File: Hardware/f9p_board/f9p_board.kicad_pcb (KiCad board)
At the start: 4 copper layers, 75 x 41 mm, 94 parts, among them J1 USB_B_Mini, J2 USB_B_Mini, J3 BAT_CONN, J4 CAN, J5 USB_A_PWR_OUTPUT, J6 EN_BAT_VIN, J7 SERV_0, J8 SERV_1, P1 SWD, Q1 DMN62D0UW-7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

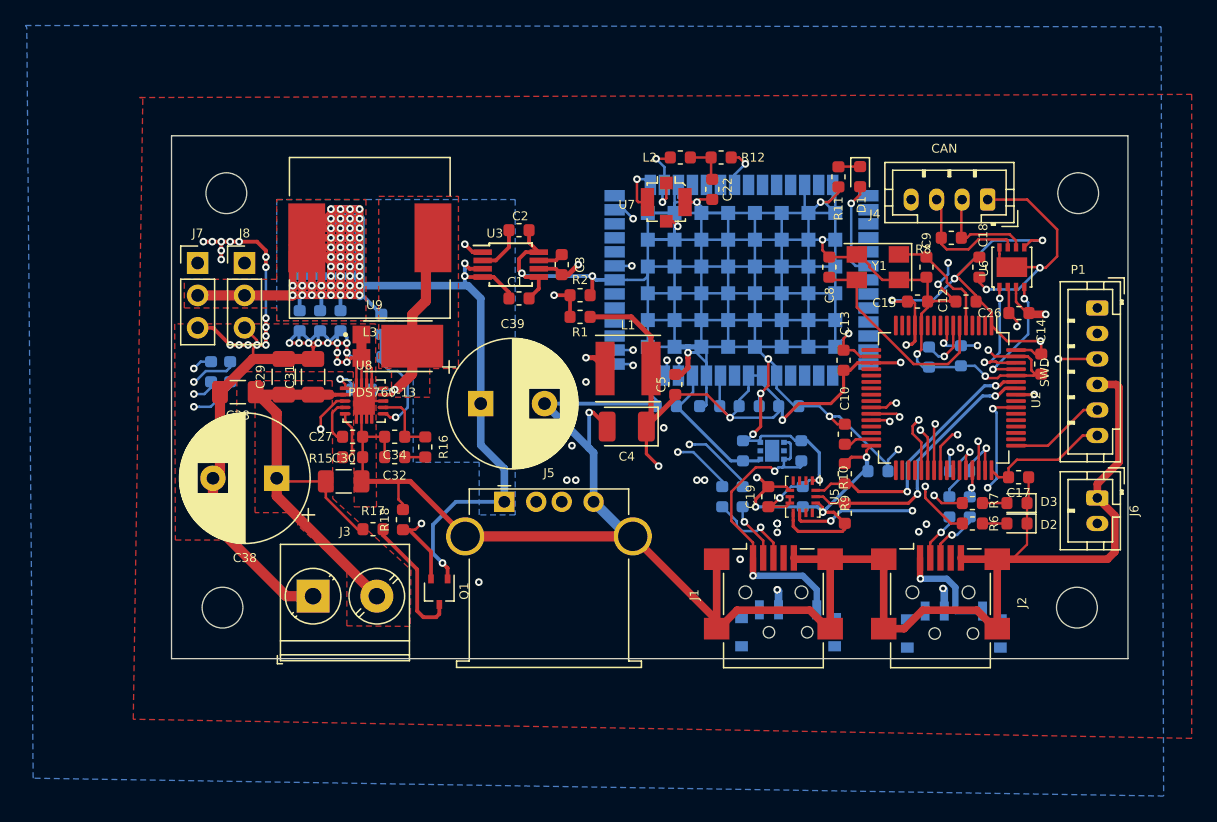
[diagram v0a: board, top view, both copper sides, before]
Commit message: f9p_board: Added switch for boot0 to enable USB flashing. Added another pair of servo connectors
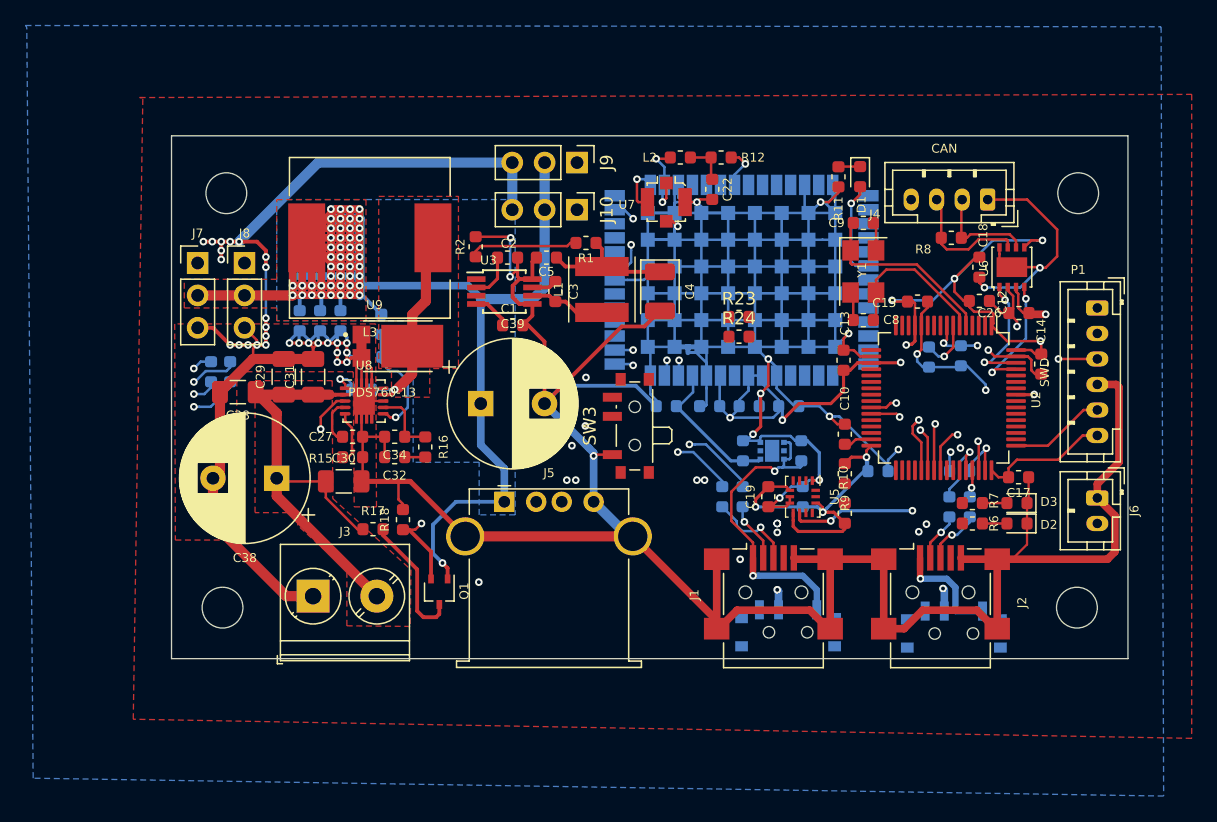
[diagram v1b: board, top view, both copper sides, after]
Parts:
- added J10: SERV_3, Connector_PinHeader_2.54mm:PinHeader_1x03_P2.54mm_Vertical, F.Cu at (76.8, 58.8)
- added J9: SERV_2, Connector_PinHeader_2.54mm:PinHeader_1x03_P2.54mm_Vertical, F.Cu at (76.8, 55.1)
- added R23: 220R, Resistor_SMD:R_0603_1608Metric, F.Cu at (89.5, 67.2)
- added R24: 220R, Resistor_SMD:R_0603_1608Metric, F.Cu at (89.5, 68.8)
- added SW3: BOOT0, Button_Switch_SMD:SW_SPDT_PCM12, F.Cu at (81.0, 75.8)
- moved C5 14.2 mm to (74.4, 62.5), turned to 180 degrees
- moved C4 10.9 mm to (83.3, 65.2), turned to -90 degrees
- moved R2 9.03 mm to (68.8, 61.7), turned to -90 degrees
- moved L1 6.53 mm to (78.8, 65.0), turned to -90 degrees
- moved C9 6.05 mm to (99.2, 59.8), turned to 180 degrees
- moved R1 5.82 mm to (77.5, 61.4)
- moved C8 4.93 mm to (99.2, 67.5), turned to 0 degrees
- moved C2 2.33 mm to (71.3, 62.5)
- moved C3 2.17 mm to (75.1, 65.2)
- moved U3 2.17 mm to (71.1, 65.2)
- moved C1 2.17 mm to (71.8, 67.9)
- moved Y1 1.19 mm to (99.2, 63.6), turned to -90 degrees
- moved C12 1.05 mm to (108.3, 66.0), turned to 0 degrees
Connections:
- U2 pad 16: Net-(U2-Pad16) -> SERV_2
- U2 pad 17: Net-(U2-Pad17) -> SERV_3
- U2 pad 28: LED0 -> GND
- U2 pad 29: Net-(U2-Pad29) -> SCL
- U2 pad 30: Net-(U2-Pad30) -> SDA
- U2 pad 42: Net-(U2-Pad42) -> PWR_5V
- U2 pad 51: Net-(U2-Pad51) -> LED0
- U2 pad 52: Net-(U2-Pad52) -> LED1
- U2 pad 55: LED1 -> Net-(U2-Pad55)
- U2 pad 58: SCL -> Net-(U2-Pad58)
- U2 pad 59: SDA -> Net-(U2-Pad59)
- U2 pad 60: GND -> Net-(SW3-Pad2)
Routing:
- net GND: track 622.0 -> 650.7 mm, vias 54 -> 50
- net VCC: track 151.6 -> 129.1 mm, vias 13 -> 11
- net SCL: track 21.2 -> 0.00 mm, vias 2 -> 0
- net SDA: track 21.1 -> 0.00 mm, vias 2 -> 0
- net LED1: track 15.4 -> 0.00 mm, vias 3 -> 0
- net LED0: track 12.4 -> 0.00 mm, vias 2 -> 0
- net PWR_5V: track 346.0 -> 356.5 mm, vias 63 -> 61
- net Net-(C3-Pad2): track 13.0 -> 5.99 mm, vias 2 -> 0
- net Net-(C9-Pad2): track 9.27 -> 14.9 mm
- net Net-(R1-Pad1): track 13.3 -> 8.57 mm, vias 2 -> 0
- net Net-(C8-Pad2): track 16.8 -> 12.5 mm
- net F9P_RESET_N: track 36.6 -> 38.8 mm
- net CAN_TX: track 9.21 -> 9.76 mm
- net Net-(R22-Pad2): track 63.2 -> 62.6 mm

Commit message: f9p_board: routing
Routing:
- net GND: track 650.7 -> 726.5 mm, vias 50 -> 110
- net Net-(SW3-Pad2): track 0.00 -> 35.8 mm, vias 0 -> 3
- net VCC: track 129.1 -> 160.1 mm, vias 11 -> 13
- net Net-(J9-Pad1): track 0.00 -> 18.7 mm
- net Net-(J10-Pad1): track 0.00 -> 18.0 mm
- net LED0: track 0.00 -> 14.1 mm, vias 0 -> 2
- net SERV_2: track 0.00 -> 12.4 mm
- net SCL: track 0.00 -> 11.4 mm
- net LED1: track 0.00 -> 10.1 mm, vias 0 -> 2
- net SERV_3: track 0.00 -> 10.0 mm
- net SDA: track 0.00 -> 9.46 mm
- net PWR_5V: track 356.5 -> 364.5 mm, vias 61 -> 62
- net Net-(R1-Pad1): track 8.57 -> 10.3 mm
- net MCU_TX_F9P_RX: track 31.7 -> 31.1 mm

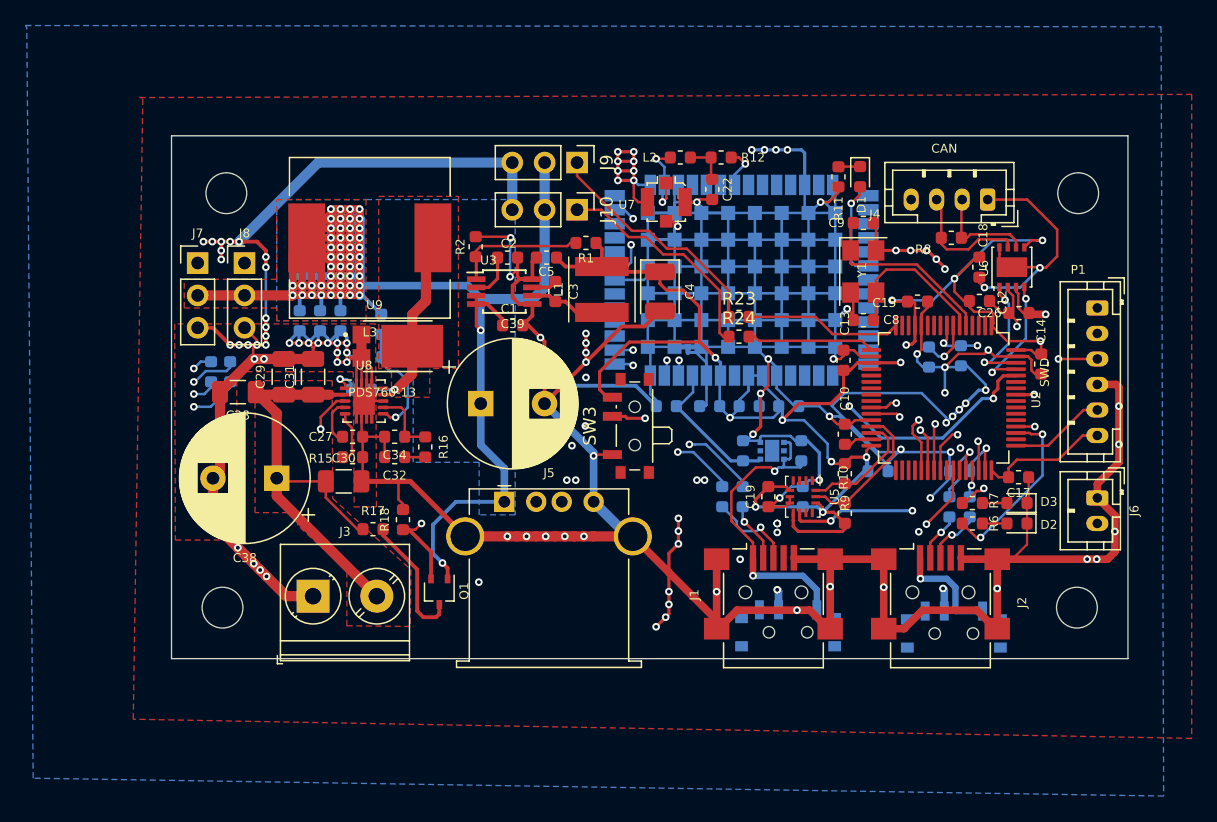
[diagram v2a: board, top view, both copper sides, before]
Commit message: f9p_board:  internal copper layers are GND
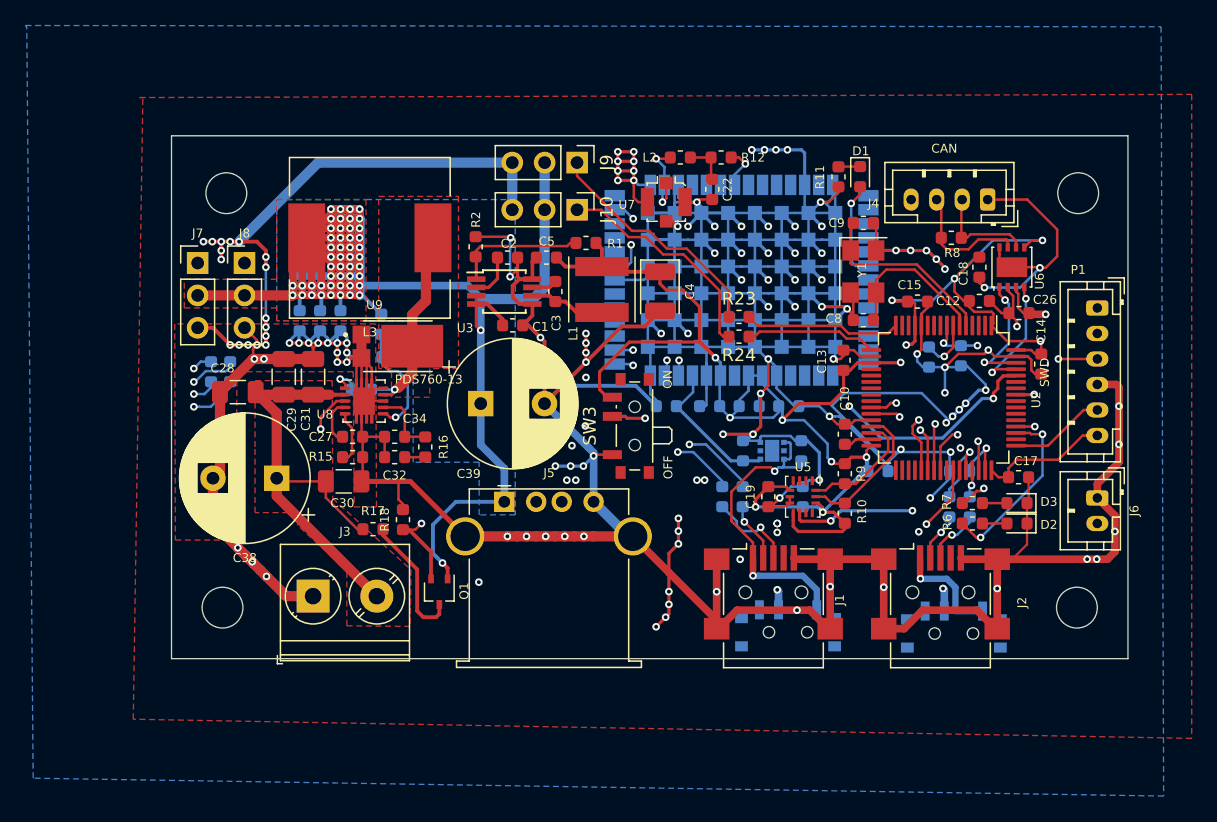
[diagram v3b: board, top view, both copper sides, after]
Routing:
- net GND: track 726.5 -> 759.0 mm, vias 110 -> 133
- added copper zone on F.Cu, net (none)
- removed copper zone on F.Cu, net SW

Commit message: Finished F9P PCB v1.0
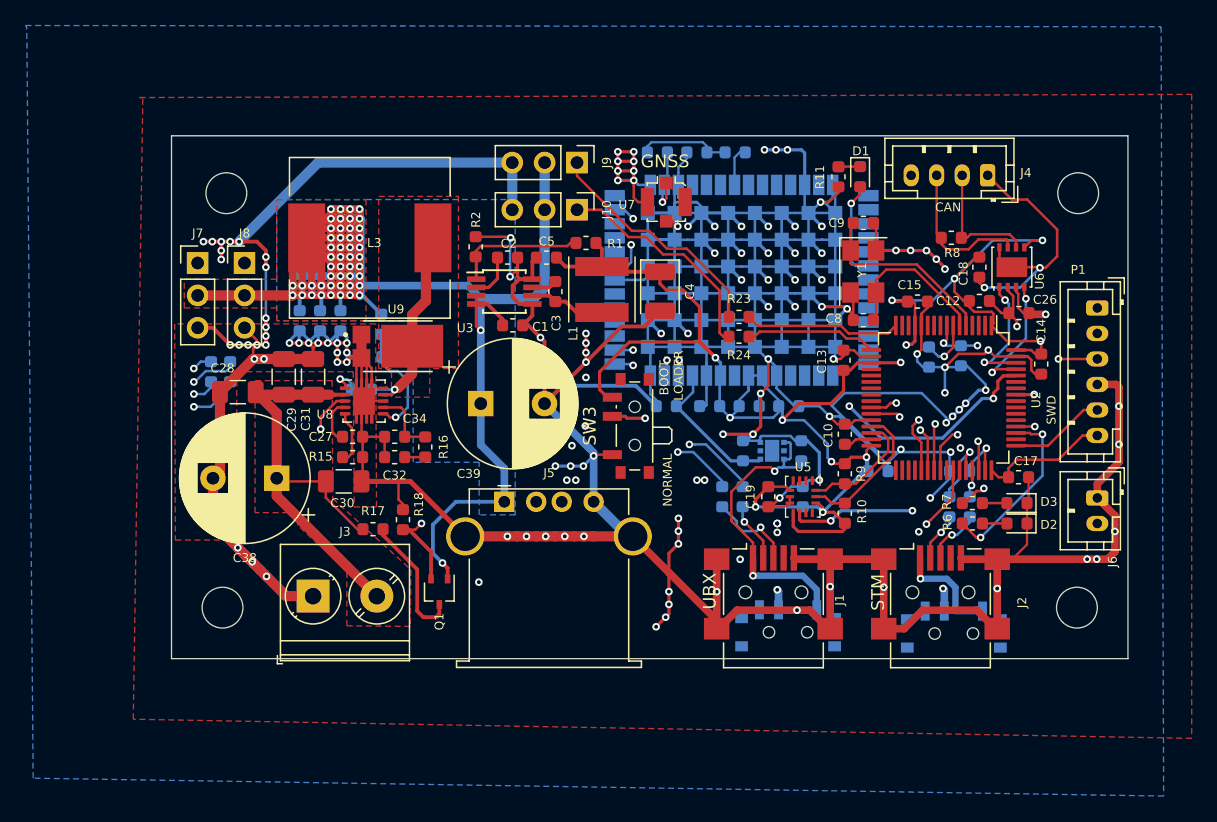
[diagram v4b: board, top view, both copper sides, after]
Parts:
- C22, L2, R12: moved to B.Cu
- moved C22 3.14 mm to (86.2, 54.3), turned to 180 degrees
- moved J4 1.90 mm to (109.0, 56.1)
- moved L2 1.84 mm to (83.1, 54.3), turned to 180 degrees
- moved R12 1.17 mm to (89.2, 54.3)
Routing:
- net Net-(C22-Pad1): track 3.37 -> 7.32 mm
- net PWR_5V: track 364.5 -> 367.5 mm
- net CANL: track 8.16 -> 10.1 mm
- net CANH: track 10.2 -> 12.1 mm
- net Net-(L2-Pad1): track 6.51 -> 5.80 mm, vias 2 -> 1
- net GND: track 759.0 -> 759.4 mm, vias 133 -> 131
- net Net-(R12-Pad1): track 3.32 -> 3.15 mm, vias 1 -> 0
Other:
- board text added: "(RX)"
- board text added: "(TX)"
- board text added: "5V"
- board text added: "7-60V"
- board text added: "BOOT- LOADER"
- board text added: "CANH"
- board text added: "CANL"
- board text added: "CarController v1.0"
- board text added: "GND"
- board text added: "GNSS"
- board text added: "Joel Svensson Benjamin Vedder"
- board text added: "NORMAL"
- board text added: "NRST"
- board text added: "PWR_OFF"
- board text added: "S"
- board text added: "STM"
- board text added: "SWCLK"
- board text added: "SWDIO"
- board text added: "UBX"
- board text added: "VCC"

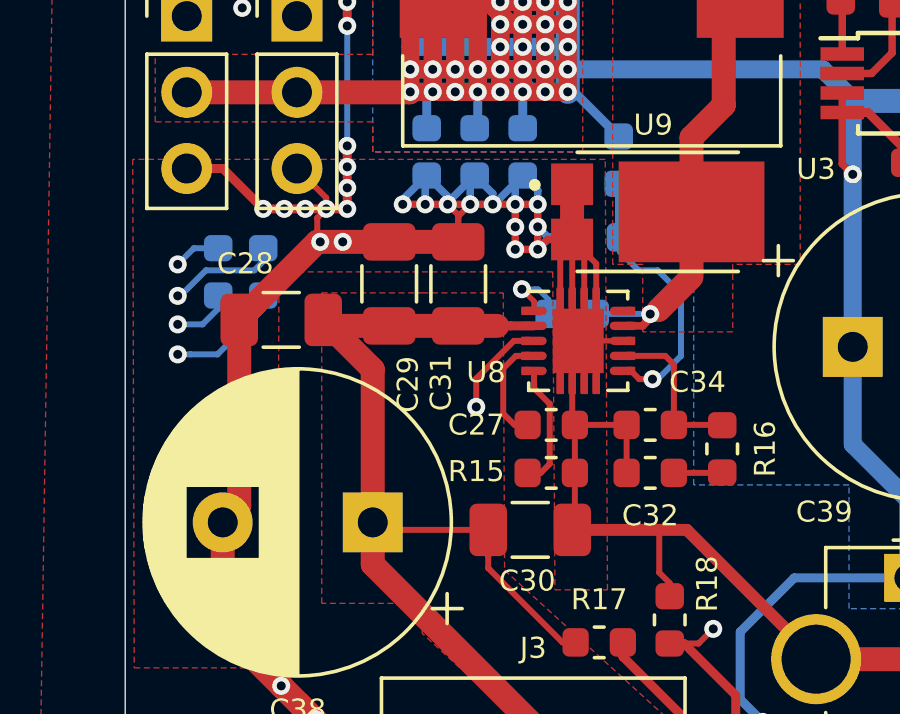
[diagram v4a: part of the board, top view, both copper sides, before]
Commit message: replacing DCDC Step-down converter footprint with - hopefully - the correct thing.
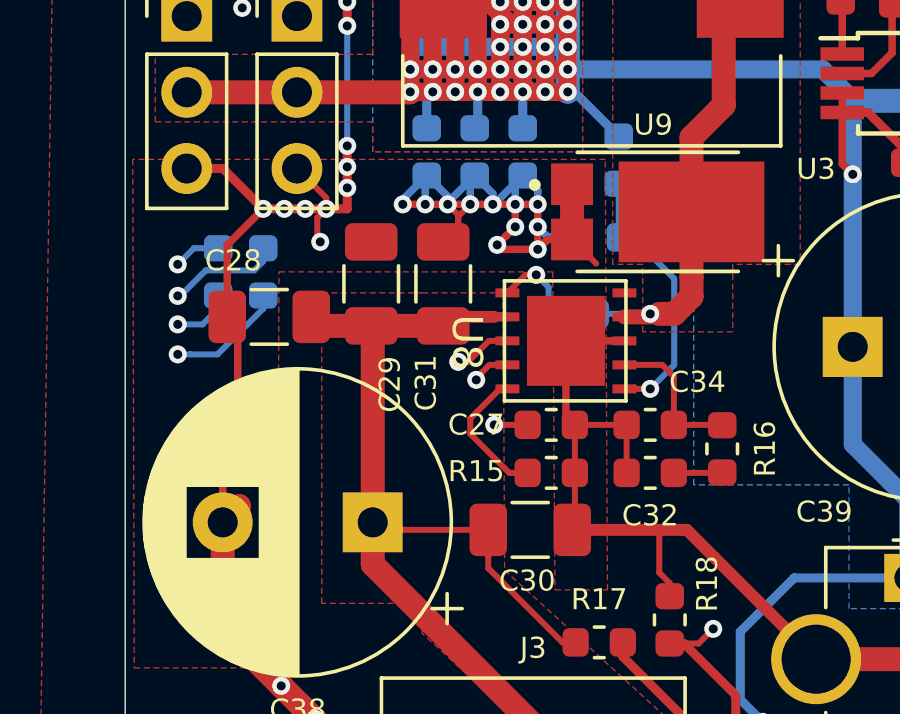
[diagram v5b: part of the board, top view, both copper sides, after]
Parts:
- U8: footprint Package_SON:Texas_S-PWSON-N10 -> f9p:TI-DPR
- moved C29 0.60 mm to (53.2, 71.9)
- moved C31 0.50 mm to (55.6, 71.9)
- moved C28 0.41 mm to (49.8, 73.0)
- moved U8 0.41 mm to (59.7, 73.8), turned to -90 degrees
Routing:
- net GND: track 759.4 -> 753.0 mm, vias 131 -> 129
- net BAT_VIN: track 38.2 -> 35.8 mm
- net Net-(R22-Pad2): track 62.6 -> 64.8 mm
- net Net-(R21-Pad2): track 60.6 -> 61.4 mm
- net SW: track 17.1 -> 17.6 mm
- net Net-(C27-Pad1): track 3.67 -> 4.14 mm, vias 0 -> 2

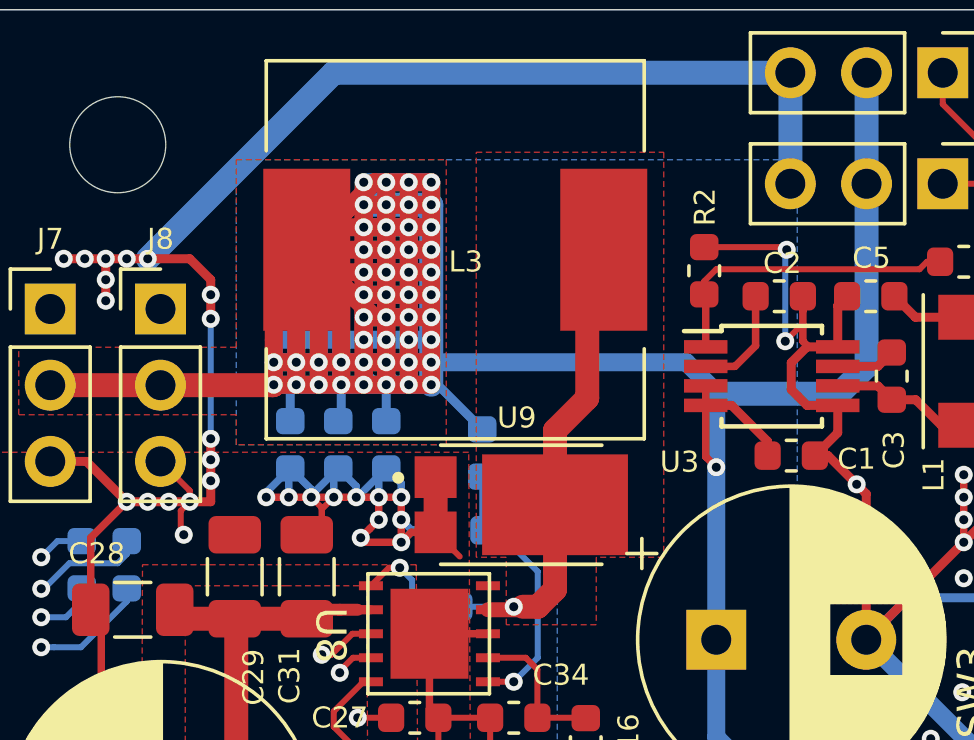
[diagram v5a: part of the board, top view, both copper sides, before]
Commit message: f9p_board: adding more Order numbers
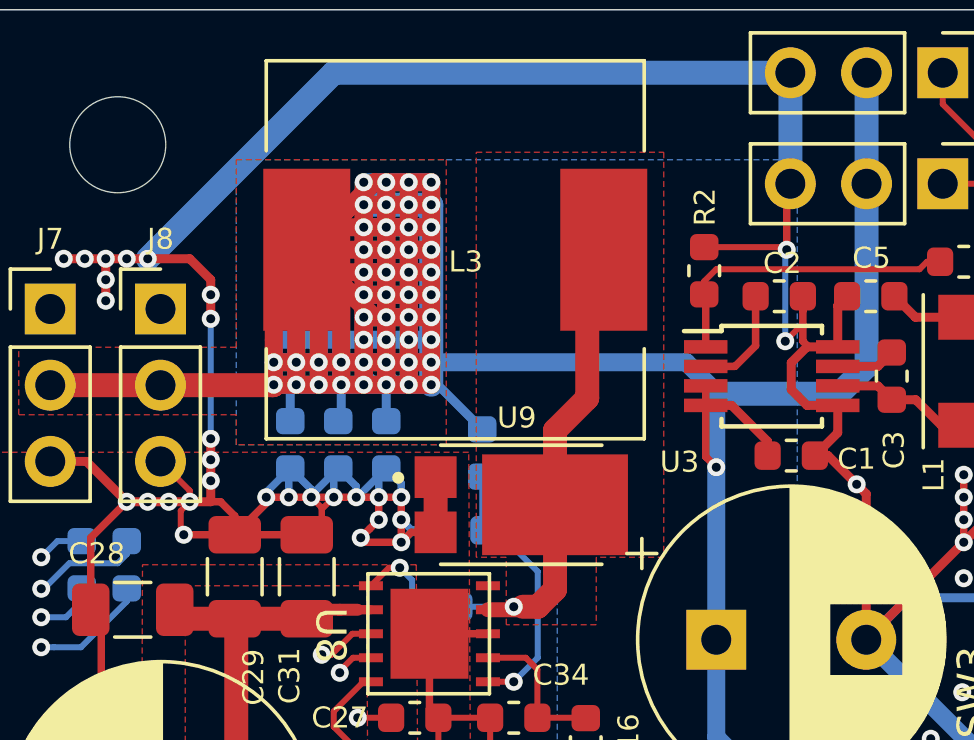
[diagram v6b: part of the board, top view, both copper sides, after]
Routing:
- net GND: track 753.0 -> 761.5 mm

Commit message: Updated F9P board
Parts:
- R13, R14: value 27 Ohm -> 22R
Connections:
- U4 pad GND: (no net) -> GND
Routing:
- net Net-(C33-Pad1): track 2.68 -> 3.44 mm
- net GND: vias 129 -> 134
- added copper zone on F.Cu, net SW
- removed copper zone on F.Cu, net (none)
